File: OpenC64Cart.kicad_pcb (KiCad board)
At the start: 2 copper layers, 58.4 x 50.8 mm, 12 parts, among them P1 CONN_01X03, P2 CONN_01X02, P3 CONN_01X02, P4 CONN_01X03, P5 CONN_01X03, P6 CONN_01X03, SW1 RESET, U1 C64-Exp-Port, U2 27512

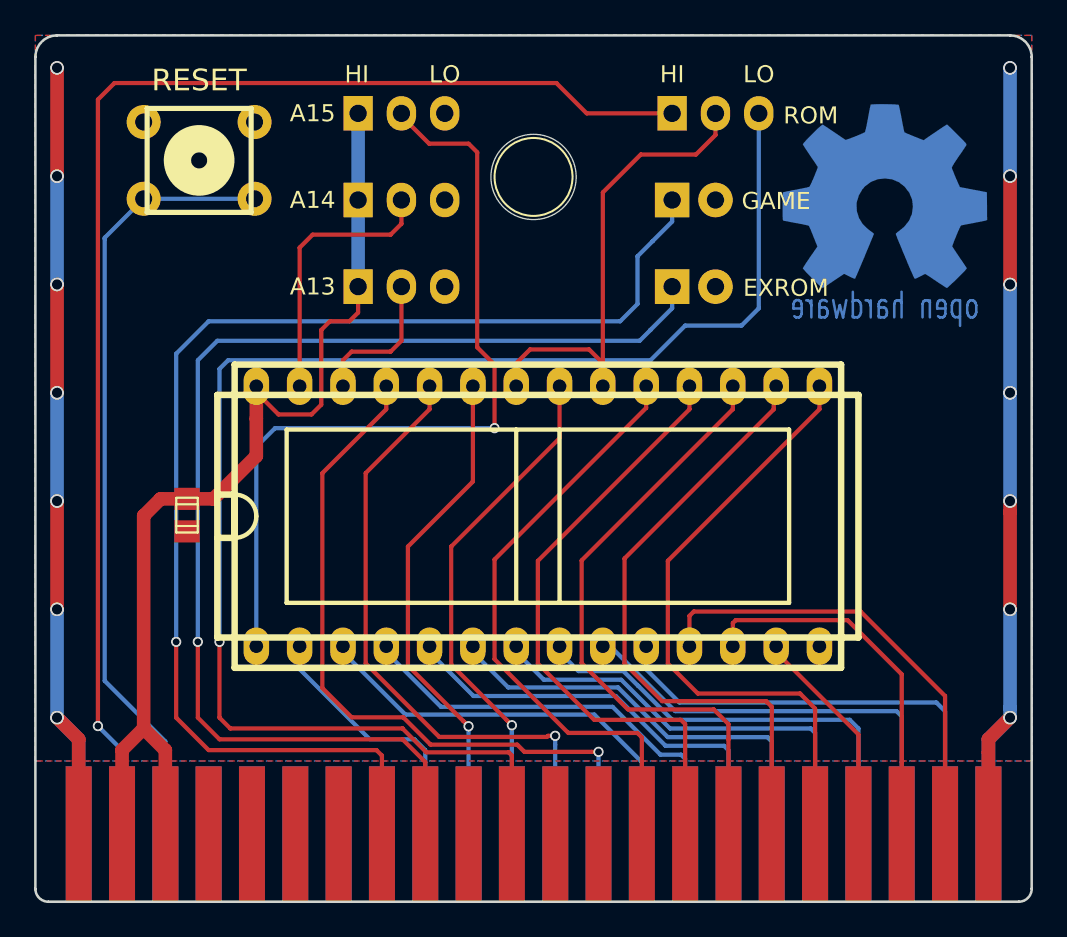
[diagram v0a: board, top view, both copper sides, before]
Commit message: Use SMD/THT combo footprint for cap, make peg hole 0.5mm bigger, fix parts for latest Kicad Thanks bigby for the peg hole size hint!
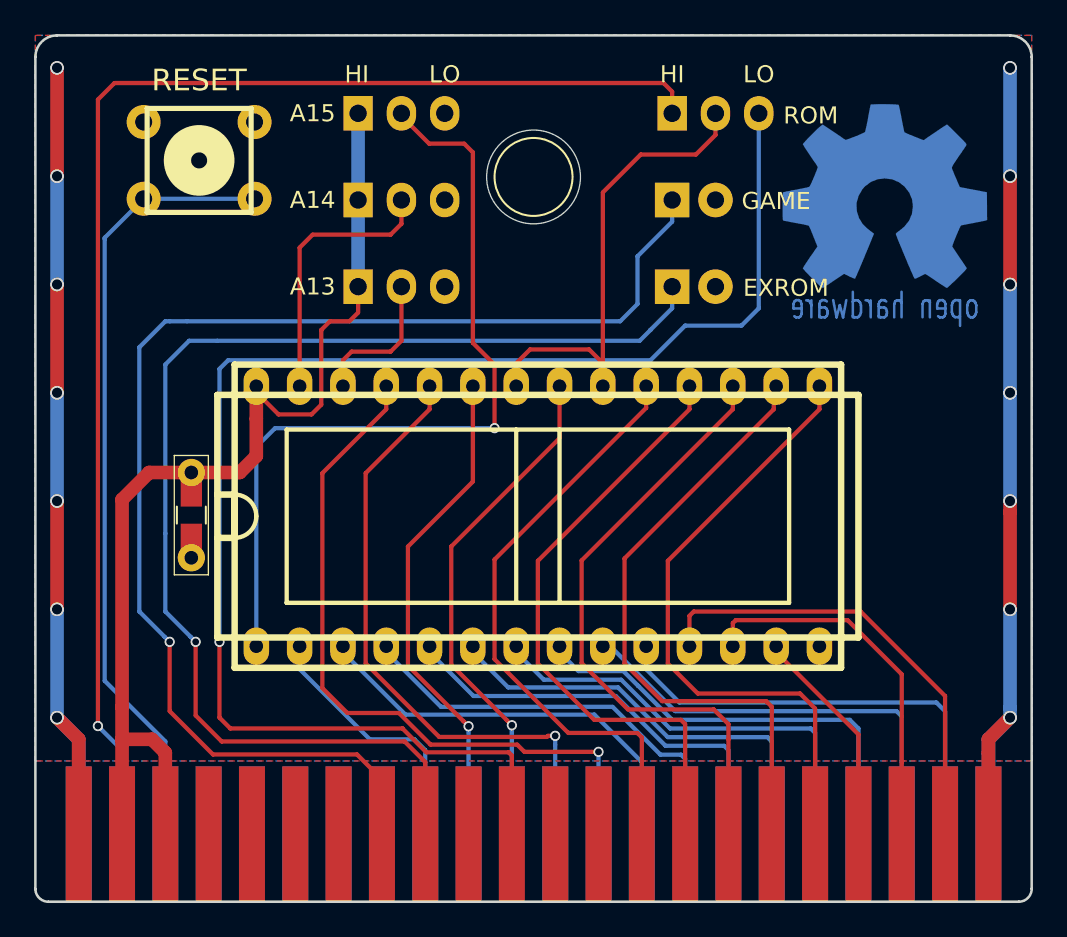
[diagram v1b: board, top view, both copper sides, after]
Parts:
- removed G***: LOGO, w_logo:Logo_copper_OSHW_12x13mm
- removed REF**: PEG_HOLE, Connectors:1pin
- added J98: OSHW_LOGO, w_logo:Logo_copper_OSHW_12x13mm, B.Cu at (109.5, 88.2)
- added J99: PEG_HOLE, Connectors:1pin, F.Cu at (88.9, 87.0)
- C1: footprint smd_cap:c_0805 -> OpenC64Cart:C_0805+THT
- P1, P4, P5, P6: footprint Sukko:Pin_Header_Straight_1x03-NoSilkS -> OpenC64Cart:Pin_Header_Straight_1x03-NoSilkS
- P2, P3: footprint Sukko:Pin_Header_Straight_1x02-NoSilkS -> OpenC64Cart:Pin_Header_Straight_1x02-NoSilkS
- SW1: footprint Sukko:PCB_PUSH -> OpenC64Cart:PCB_PUSH
- U1: footprint Sukko:C64-Cart-NoSilkS -> OpenC64Cart:C64-Cart
- moved C1 0.25 mm to (68.8, 106.9), turned to 90 degrees
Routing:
- net +5V: track 61.7 -> 65.2 mm
- net Net-(P3-Pad1): track 70.0 -> 72.5 mm
- net Net-(P2-Pad1): track 74.2 -> 76.6 mm
- net Net-(P1-Pad1): track 78.5 -> 79.2 mm

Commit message: Final touches for V2
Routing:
- net Net-(U1-Pad21): track 27.0 -> 28.9 mm
- net Net-(SW1-Pad3): track 46.2 -> 47.3 mm
- net Net-(P1-Pad2): track 29.1 -> 29.9 mm
- net Net-(P6-Pad2): track 48.2 -> 48.8 mm

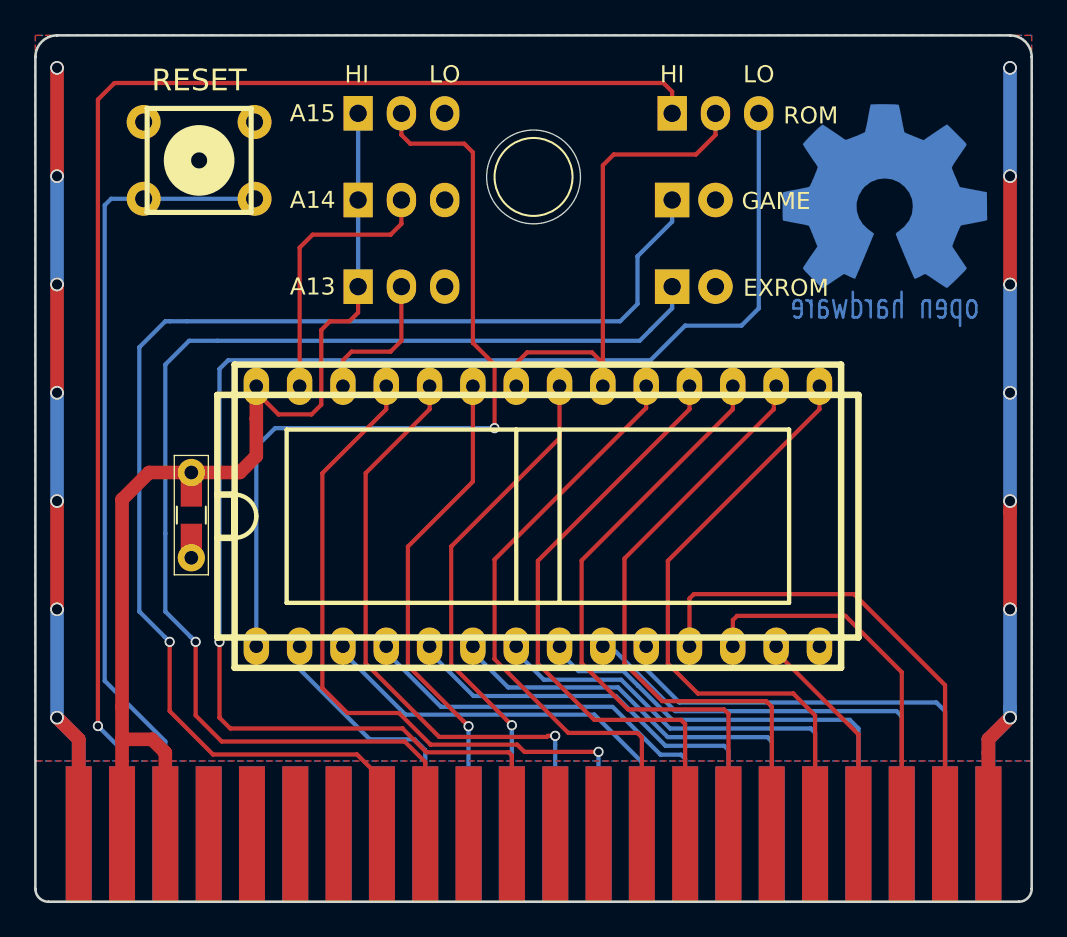
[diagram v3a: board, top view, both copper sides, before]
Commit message: Use a single jumper for GAME/EXROM
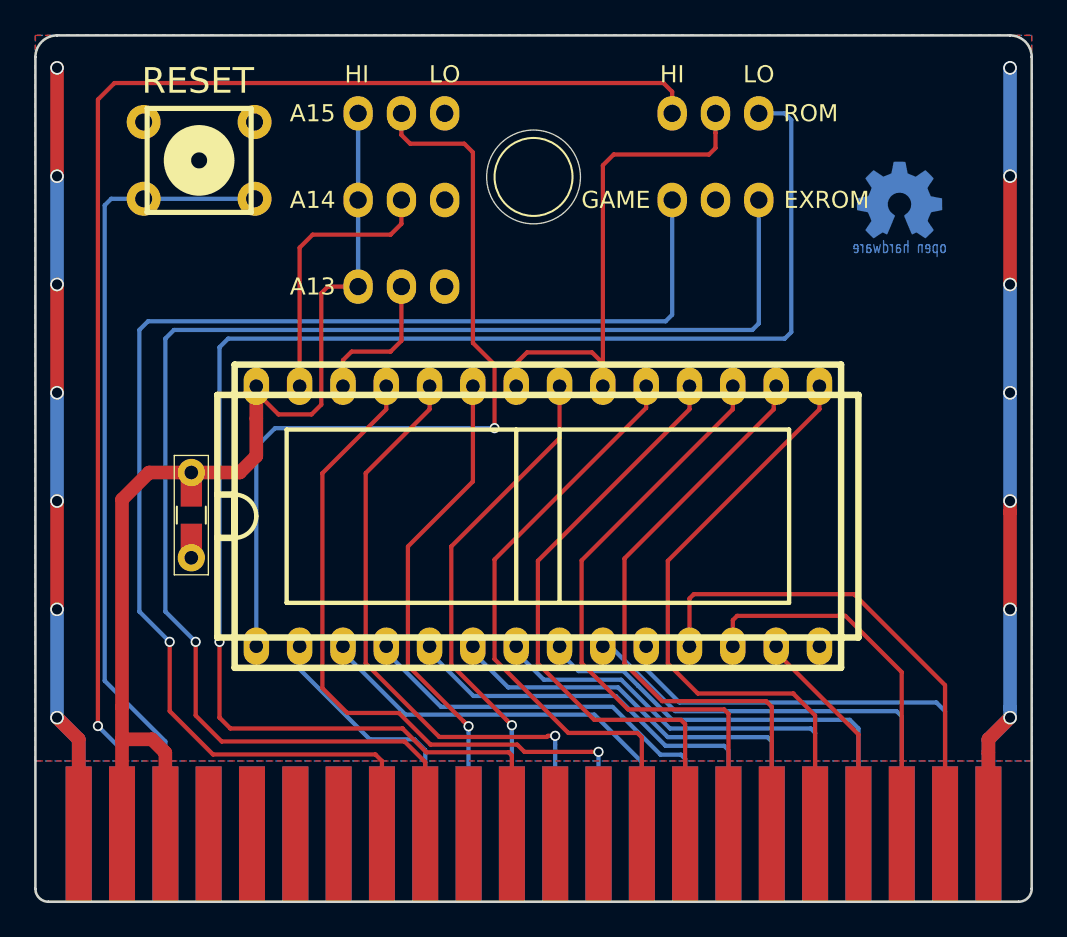
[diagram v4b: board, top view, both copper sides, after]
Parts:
- removed P3: CONN_01X02, OpenC64Cart:Pin_Header_Straight_1x02-NoSilkS
- C1: value C -> 100n
- J98: footprint w_logo:Logo_copper_OSHW_12x13mm -> w_logo:Logo_copper_OSHW_6x6mm
- P2: value CONN_01X02 -> CONN_01X03; footprint OpenC64Cart:Pin_Header_Straight_1x02-NoSilkS -> OpenC64Cart:Pin_Header_Straight_1x03-NoSilkS
- SW1: value RESET -> RESET_SW
- moved J98 0.89 mm to (110.4, 88.4)
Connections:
- U1 pad 9: Net-(P3-Pad1) -> Net-(P2-Pad3)
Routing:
- net Net-(P2-Pad3): track 0.00 -> 84.1 mm, vias 0 -> 1
- net Net-(P3-Pad1): track 72.5 -> 0.00 mm, vias 1 -> 0
- net Net-(P1-Pad3): track 87.7 -> 92.8 mm
- net Net-(P2-Pad1): track 76.6 -> 79.4 mm
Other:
- board text added: "RESET"
- board text added: "V3"
- board text removed: "V2"

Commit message: Minor adjustments. Update images.
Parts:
- moved J98 1.35 mm to (110.4, 87.0)
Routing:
- net Net-(P1-Pad1): track 79.2 -> 81.0 mm, vias 1 -> 0
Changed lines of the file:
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@@
     (thickness 1.6)
     (drawings 25)
-    (tracks 297)
+    (tracks 295)
     (zones 0)
     (modules 11)
@@
   )
   (module w_logo:Logo_copper_OSHW_6x6mm (layer B.Cu)
-    (at 110.363 88.392 180)
+    (at 110.363 87.04 180)
     (descr "Open Hardware Logo, 6x6mm")
     (fp_text reference J98 (at 0 0 180) (layer B.SilkS) hide
@@
   (via (at 60.96 118.745) (size 0.8) (drill 0.6) (layers F.Cu B.Cu) (net 1))
   (segment (start 62.23 125.601726) (end 62.23 120.015) (width 0.8) (layer F.Cu) (net 1))
-  (segment (start 78.613 93.472) (end 76.835 93.472) (width 0.25) (layer F.Cu) (net 2))
-  (segment (start 76.835 93.472) (end 76.454 93.853) (width 0.25) (layer F.Cu) (net 2))
-  (segment (start 76.454 93.853) (end 76.454 100.3935) (width 0.25) (layer F.Cu) (net 2))
-  (segment (start 76.454 100.3935) (end 75.8825 100.965) (width 0.25) (layer F.Cu) (net 2))
-  (segment (start 75.8825 100.965) (end 73.94575 100.965) (width 0.25) (layer F.Cu) (net 2))
-  (segment (start 73.94575 100.965) (end 72.644 99.66325) (width 0.25) (layer F.Cu) (net 2))
+  (segment (start 74.07275 101.092) (end 76.2 101.092) (width 0.25) (layer F.Cu) (net 2))
+  (segment (start 76.581 100.711) (end 76.581 93.853) (width 0.25) (layer F.Cu) (net 2))
+  (segment (start 76.2 101.092) (end 76.581 100.711) (width 0.25) (layer F.Cu) (net 2))
+  (segment (start 72.644 99.314) (end 72.644 99.66325) (width 0.25) (layer F.Cu) (net 2))
+  (segment (start 72.644 99.66325) (end 74.07275 101.092) (width 0.25) (layer F.Cu) (net 2))
+  (segment (start 76.962 93.472) (end 78.613 93.472) (width 0.25) (layer F.Cu) (net 2))
+  (segment (start 76.581 93.853) (end 76.962 93.472) (width 0.25) (layer F.Cu) (net 2))
   (segment (start 68.834 105.6205) (end 68.834 104.3705) (width 0.8) (layer F.Cu) (net 2))
   (segment (start 64.77 118.11) (end 64.77 105.96) (width 0.8) (layer F.Cu) (net 2))
@@
   (segment (start 64.77 105.96) (end 66.3595 104.3705) (width 0.8) (layer F.Cu) (net 2))
   (segment (start 66.3595 104.3705) (end 68.58 104.3705) (width 0.8) (layer F.Cu) (net 2))
-  (segment (start 72.644 99.314) (end 72.644 99.66325) (width 0.8) (layer F.Cu) (net 2))
   (segment (start 78.613 88.392) (end 78.613 83.312) (width 0.254) (layer B.Cu) (net 2))
   (segment (start 78.613 88.392) (end 78.613 93.472) (width 0.254) (layer B.Cu) (net 2))
   (segment (start 72.644 101.21382) (end 72.644 99.314) (width 0.8) (layer F.Cu) (net 2))
   (segment (start 72.644 103.4033) (end 72.644 101.21382) (width 0.8) (layer F.Cu) (net 2))
-  (segment (start 63.356609 119.236609) (end 63.356609 82.502891) (width 0.25) (layer F.Cu) (net 3))
-  (segment (start 63.356609 82.502891) (end 64.3255 81.534) (width 0.25) (layer F.Cu) (net 3))
-  (segment (start 64.3255 81.534) (end 96.52 81.534) (width 0.25) (layer F.Cu) (net 3))
-  (segment (start 96.52 81.534) (end 97.028 82.042) (width 0.25) (layer F.Cu) (net 3))
-  (segment (start 97.028 82.042) (end 97.028 83.312) (width 0.25) (layer F.Cu) (net 3))
-  (segment (start 63.356609 119.236609) (end 64.77 120.65) (width 0.25) (layer B.Cu) (net 3))
-  (segment (start 64.77 120.65) (end 64.77 125.601726) (width 0.25) (layer B.Cu) (net 3))
-  (via (at 63.356609 119.236609) (size 0.6) (drill 0.4) (layers F.Cu B.Cu) (net 3))
-  (segment (start 99.568 84.455) (end 99.568 83.312) (width 0.25) (layer F.Cu) (net 4))
-  (segment (start 92.964 99.314) (end 92.964 86.36) (width 0.25) (layer F.Cu) (net 4))
-  (segment (start 99.568 85.344) (end 99.568 84.455) (width 0.25) (layer F.Cu) (net 4))
-  (segment (start 99.187 85.725) (end 99.568 85.344) (width 0.25) (layer F.Cu) (net 4))
-  (segment (start 93.599 85.725) (end 99.187 85.725) (width 0.25) (layer F.Cu) (net 4))
-  (segment (start 92.964 86.36) (end 93.599 85.725) (width 0.25) (layer F.Cu) (net 4))
+  (segment (start 64.77 125.601726) (end 64.77 120.65) (width 0.25) (layer B.Cu) (net 3))
+  (segment (start 64.77 120.65) (end 62.23 118.11) (width 0.25) (layer B.Cu) (net 3))
+  (segment (start 62.23 118.11) (end 62.23 82.169) (width 0.25) (layer B.Cu) (net 3))
+  (segment (start 62.23 82.169) (end 62.865 81.534) (width 0.25) (layer B.Cu) (net 3))
+  (segment (start 62.865 81.534) (end 96.52 81.534) (width 0.25) (layer B.Cu) (net 3))
+  (segment (start 96.52 81.534) (end 97.028 82.042) (width 0.25) (layer B.Cu) (net 3))
+  (segment (start 97.028 82.042) (end 97.028 83.312) (width 0.25) (layer B.Cu) (net 3))
+  (segment (start 92.964 99.314) (end 92.964 85.598) (width 0.25) (layer F.Cu) (net 4))
+  (segment (start 92.964 85.598) (end 93.472 85.09) (width 0.25) (layer F.Cu) (net 4))
+  (segment (start 93.472 85.09) (end 99.056 85.09) (width 0.25) (layer F.Cu) (net 4))
+  (segment (start 99.056 85.09) (end 99.568 84.578) (width 0.25) (layer F.Cu) (net 4))
+  (segment (start 99.568 84.578) (end 99.568 83.312) (width 0.25) (layer F.Cu) (net 4))
   (segment (start 87.884 97.96418) (end 88.519 97.32918) (width 0.25) (layer F.Cu) (net 4))
   (segment (start 92.329 97.32918) (end 92.964 97.96418) (width 0.25) (layer F.Cu) (net 4))
@@
   (segment (start 67.31 125.601726) (end 67.31 120.142) (width 0.25) (layer B.Cu) (net 31))
   (segment (start 67.31 120.142) (end 63.754 116.586) (width 0.25) (layer B.Cu) (net 31))
-  (segment (start 63.754 116.586) (end 63.754 88.70188) (width 0.25) (layer B.Cu) (net 31))
-  (segment (start 63.754 88.70188) (end 64.135 88.32088) (width 0.25) (layer B.Cu) (net 31))
-  (segment (start 64.135 88.32088) (end 66.04 88.32088) (width 0.25) (layer B.Cu) (net 31))
+  (segment (start 63.754 116.586) (end 63.754 88.82888) (width 0.25) (layer B.Cu) (net 31))
+  (segment (start 63.754 88.82888) (end 64.262 88.32088) (width 0.25) (layer B.Cu) (net 31))
+  (segment (start 64.262 88.32088) (end 66.04 88.32088) (width 0.25) (layer B.Cu) (net 31))
   (segment (start 66.04 88.32088) (end 72.5424 88.32088) (width 0.25) (layer B.Cu) (net 31))
   (segment (start 69.088 114.3) (end 67.31 112.522) (width 0.25) (layer B.Cu) (net 32))
